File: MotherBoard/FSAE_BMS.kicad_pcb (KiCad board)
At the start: 2 copper layers, 2 parts, among them J1 1376357-3, U1 STM32F205RBTx

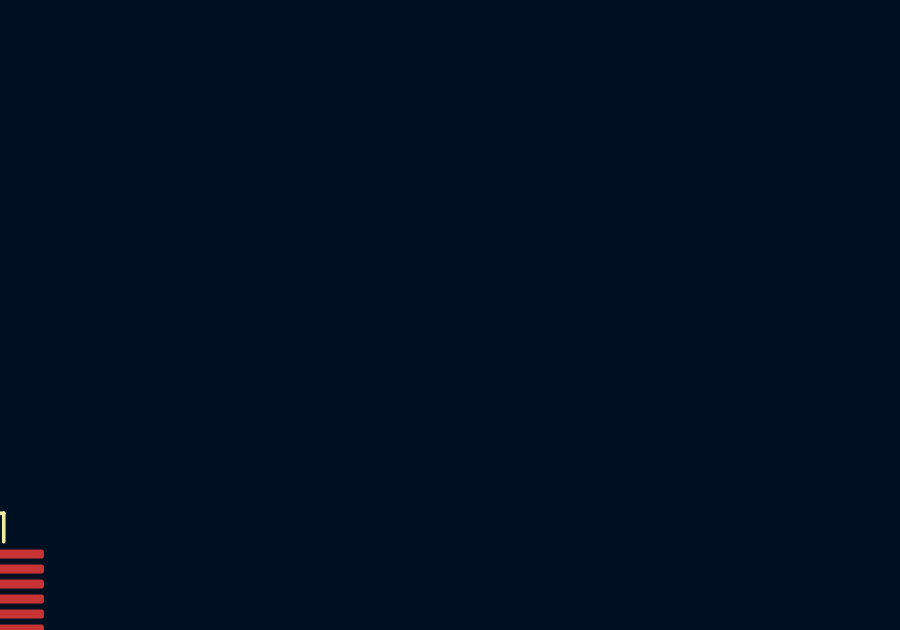
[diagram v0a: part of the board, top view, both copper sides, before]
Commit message: Complete bootstrap schematic for MCU
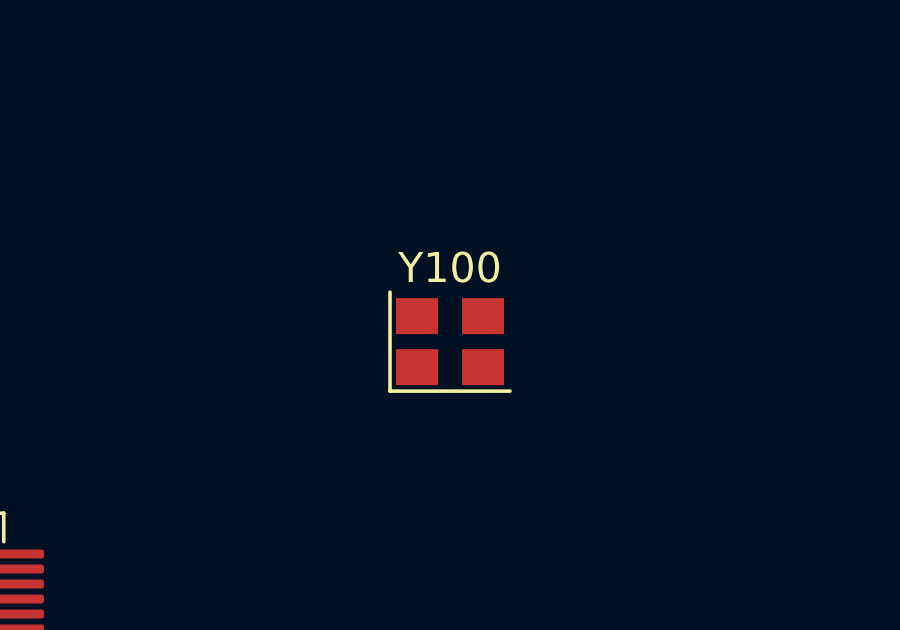
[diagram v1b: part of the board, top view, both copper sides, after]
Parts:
- added Y100: 16 Mhz, Crystal:Crystal_SMD_3225-4Pin_3.2x2.5mm, F.Cu at (136.3, 66.9)
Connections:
- U1 pad 12: unconnected-(U1-VSSA-Pad12) -> GND
- U1 pad 14: unconnected-(U1-PA0-Pad14) -> ADC3_IN0
- U1 pad 15: unconnected-(U1-PA1-Pad15) -> ADC3_IN1
- U1 pad 18: Net-(U1-VSS-Pad18) -> GND
- U1 pad 21: unconnected-(U1-PA5-Pad21) -> SPI1_SCK
- U1 pad 22: unconnected-(U1-PA6-Pad22) -> SPI1_MISO
- U1 pad 23: unconnected-(U1-PA7-Pad23) -> SPI1_MOSI
- U1 pad 24: unconnected-(U1-PC4-Pad24) -> CHARGE_EN_LV
- U1 pad 25: unconnected-(U1-PC5-Pad25) -> DISCHARGE_EN_LV
- U1 pad 26: unconnected-(U1-PB0-Pad26) -> CHARGE_SAFE_LV
- U1 pad 27: unconnected-(U1-PB1-Pad27) -> CHARGE_PWR_CTRL
- U1 pad 28: unconnected-(U1-PB2-Pad28) -> READY_PWR_CTRL
- U1 pad 29: unconnected-(U1-PB10-Pad29) -> FAN_EN
- U1 pad 33: unconnected-(U1-PB12-Pad33) -> CAN2_RX
- U1 pad 34: unconnected-(U1-PB13-Pad34) -> CAN2_TX
- U1 pad 39: unconnected-(U1-PC8-Pad39) -> SDIO_D0
- U1 pad 40: unconnected-(U1-PC9-Pad40) -> SDIO_D1
- U1 pad 41: unconnected-(U1-PA8-Pad41) -> FAN_PWM
- U1 pad 44: unconnected-(U1-PA11-Pad44) -> CAN1_RX
- U1 pad 45: unconnected-(U1-PA12-Pad45) -> CAN1_TX
- U1 pad 46: unconnected-(U1-PA13-Pad46) -> /MCU/SWDIO
- U1 pad 49: unconnected-(U1-PA14-Pad49) -> /MCU/SWCLK
- U1 pad 51: unconnected-(U1-PC10-Pad51) -> SDIO_D2
- U1 pad 52: unconnected-(U1-PC11-Pad52) -> SDIO_D3
- U1 pad 53: unconnected-(U1-PC12-Pad53) -> SDIO_CK
- U1 pad 54: unconnected-(U1-PD2-Pad54) -> SDIO_CMD
- U1 pad 55: unconnected-(U1-PB3-Pad55) -> /MCU/SWO
- U1 pad 63: Net-(U1-VSS-Pad18) -> GND

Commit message: PSU Complete
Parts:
- removed J1: 1376357-3, IO:13763573
- removed U1: STM32F205RBTx, Package_QFP:LQFP-64_10x10mm_P0.5mm
- removed Y100: 16 Mhz, Crystal:Crystal_SMD_3225-4Pin_3.2x2.5mm
- added D201: D_TVS, Diode_SMD:D_SOD-323, F.Cu at (89.1, 47.0)
- added D202: D_TVS, Diode_SMD:D_SOD-323, F.Cu at (89.1, 53.9)
- added D203: D_TVS, Diode_SMD:D_SOD-323, F.Cu at (89.1, 60.7)
- added D204: D_TVS, Diode_SMD:D_SOD-323, F.Cu at (89.1, 67.6)
- added D205: D_TVS, Diode_SMD:D_SOD-323, F.Cu at (89.1, 74.4)
- added D206: D_TVS, Diode_SMD:D_SOD-323, F.Cu at (89.1, 81.3)
- added D207: D_TVS, Diode_SMD:D_SOD-323, F.Cu at (89.1, 88.1)
- added D208: D_TVS, Diode_SMD:D_SOD-323, F.Cu at (89.1, 95.0)
- added D209: D_TVS, Diode_SMD:D_SOD-323, F.Cu at (89.1, 101.8)
- added D210: D_TVS, Diode_SMD:D_SOD-323, F.Cu at (89.1, 108.7)
- added D211: D_TVS, Diode_SMD:D_SOD-323, F.Cu at (89.1, 115.5)
- added D212: D_TVS, Diode_SMD:D_SOD-323, F.Cu at (89.1, 122.4)
- added D213: D_TVS, Diode_SMD:D_SOD-323, F.Cu at (89.1, 129.2)
- added J201: Conn_ARM_SWD_TagConnect_TC2030, Connector:Tag-Connect_TC2030-IDC-FP_2x03_P1.27mm_Vertical, F.Cu at (111.2, 62.8)
- added J301: 1376357-3, IO:13763573, F.Cu at (125.4, 49.8)
- added L402: 22u, SW_Inductor:IND_IHLP-6767DZ_VIS, F.Cu at (176.1, 58.2)
- added L403: 22u, SW_Inductor:IND_IHLP-6767DZ_VIS, F.Cu at (176.1, 77.0)
- added R201: 10k, Resistor_SMD:R_0402_1005Metric, F.Cu at (49.6, 50.1)
- added R202: 0R, Resistor_SMD:R_0402_1005Metric, F.Cu at (49.6, 52.1)
- added R203: 22R, Resistor_SMD:R_0402_1005Metric, F.Cu at (49.6, 54.1)
- added R204: 22R, Resistor_SMD:R_0402_1005Metric, F.Cu at (49.6, 56.1)
- added R205: 22R, Resistor_SMD:R_0402_1005Metric, F.Cu at (49.6, 58.0)
- added R206: 22R, Resistor_SMD:R_0402_1005Metric, F.Cu at (52.5, 50.1)
- added R207: 10k, Resistor_SMD:R_0402_1005Metric, F.Cu at (52.5, 52.1)
- added R208: 10k, Resistor_SMD:R_0402_1005Metric, F.Cu at (52.5, 54.1)
- added R209: 10k, Resistor_SMD:R_0402_1005Metric, F.Cu at (52.5, 56.1)
- added R210: 10k, Resistor_SMD:R_0402_1005Metric, F.Cu at (52.5, 58.0)
- added R211: 10k, Resistor_SMD:R_0402_1005Metric, F.Cu at (55.5, 50.1)
- added R212: 10k, Resistor_SMD:R_0402_1005Metric, F.Cu at (55.5, 52.1)
- added R213: 22R, Resistor_SMD:R_0402_1005Metric, F.Cu at (55.5, 54.1)
- added R214: 1M, Resistor_SMD:R_0402_1005Metric, F.Cu at (55.5, 56.1)
- added R401: 100k, Resistor_SMD:R_0402_1005Metric, F.Cu at (44.7, 50.1)
- added R402: 22.1k, Resistor_SMD:R_0402_1005Metric, F.Cu at (44.7, 52.1)
- added R403: 162k, Resistor_SMD:R_0402_1005Metric, F.Cu at (44.7, 54.1)
- added R404: 22.1k, Resistor_SMD:R_0402_1005Metric, F.Cu at (44.7, 56.1)
- added R405: 1k, Resistor_SMD:R_0402_1005Metric, F.Cu at (44.7, 58.0)
- added R406: 1k, Resistor_SMD:R_0402_1005Metric, F.Cu at (44.7, 60.0)
- added U201: STM32F205RBTx, Package_QFP:LQFP-64_10x10mm_P0.5mm, F.Cu at (113.6, 50.8)
- added U401: LMR51430, Package_TO_SOT_SMD:SOT-23-6, F.Cu at (125.4, 93.6)
- added U402: LMR51430, Package_TO_SOT_SMD:SOT-23-6, F.Cu at (125.4, 98.2)
- added Y201: 16 Mhz, Crystal:Crystal_SMD_3225-4Pin_3.2x2.5mm, F.Cu at (118.1, 60.3)

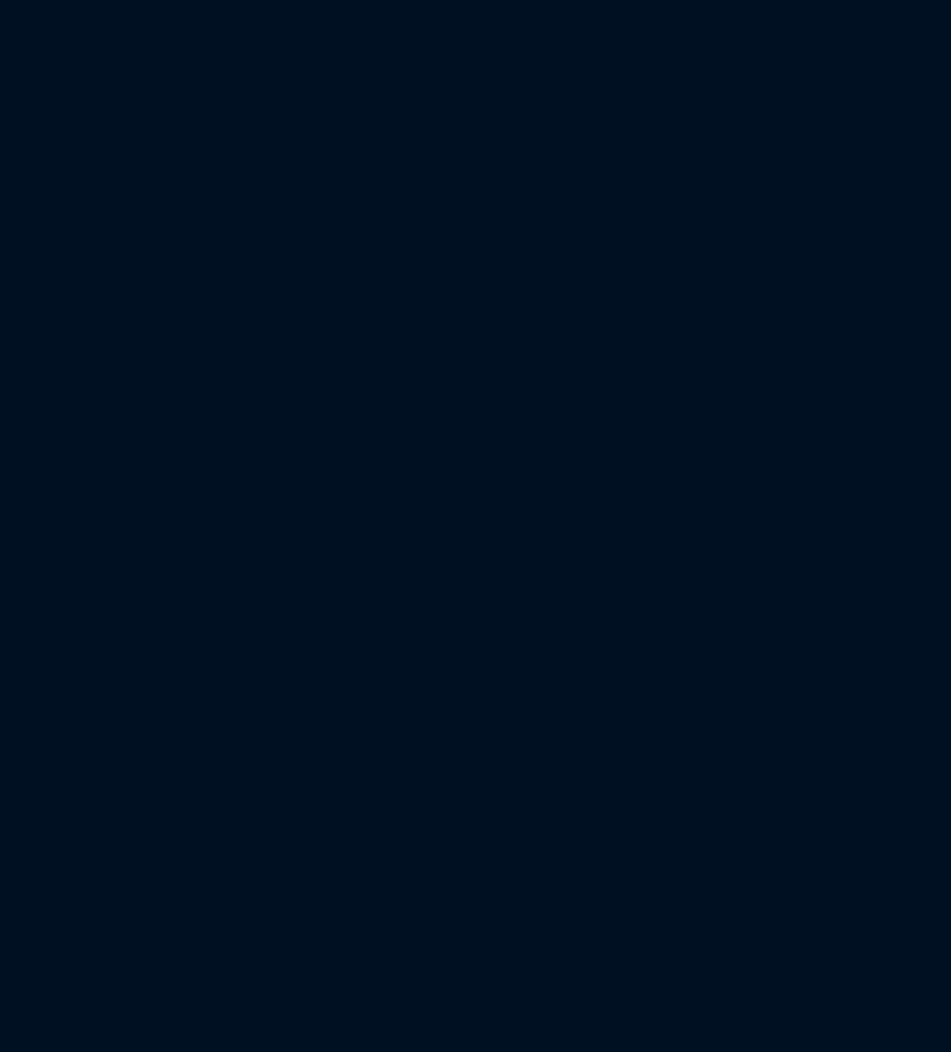
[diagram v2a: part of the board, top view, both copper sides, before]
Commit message: Added BQ7900 rough draft and TCAN
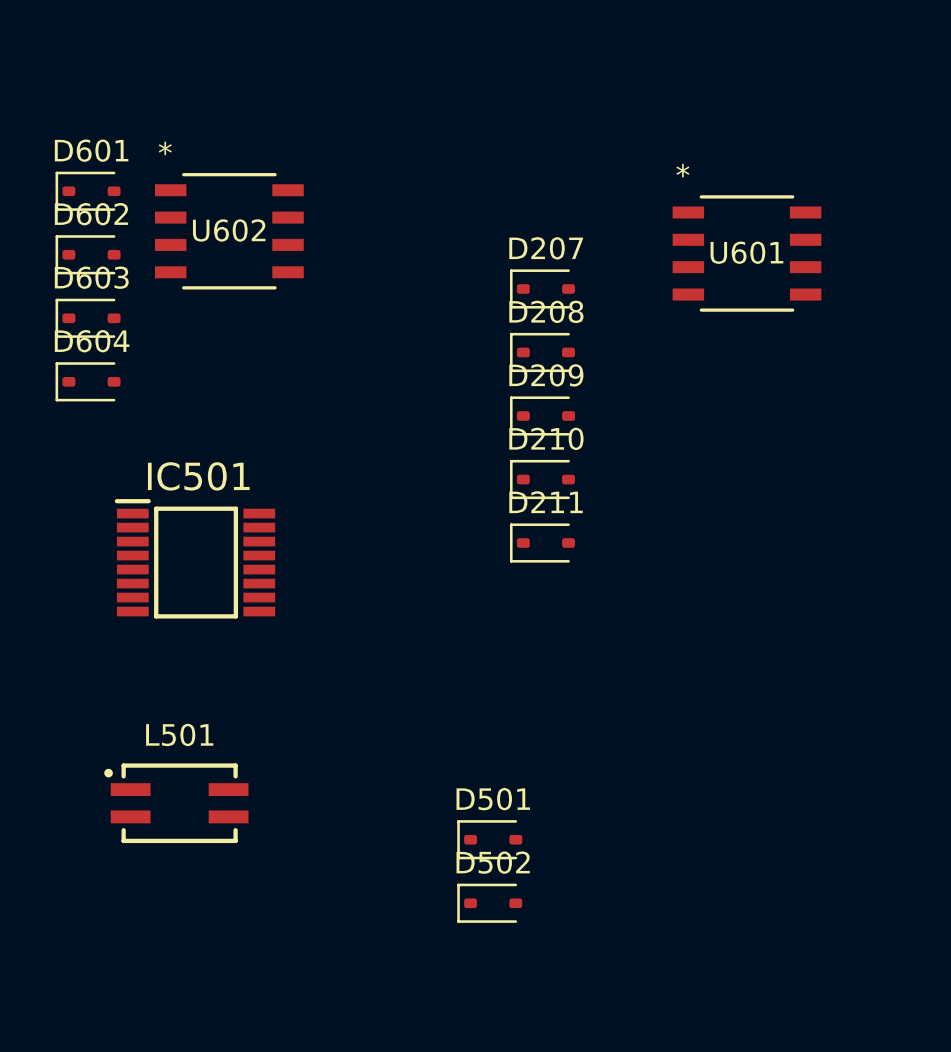
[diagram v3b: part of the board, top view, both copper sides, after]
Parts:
- added D207: D_TVS, Diode_SMD:D_SOD-323, F.Cu at (61.6, 76.1)
- added D208: D_TVS, Diode_SMD:D_SOD-323, F.Cu at (61.6, 79.1)
- added D209: D_TVS, Diode_SMD:D_SOD-323, F.Cu at (61.6, 82.0)
- added D210: D_TVS, Diode_SMD:D_SOD-323, F.Cu at (61.6, 85.0)
- added D211: D_TVS, Diode_SMD:D_SOD-323, F.Cu at (61.6, 87.9)
- added D501: D_TVS, Diode_SMD:D_SOD-323, F.Cu at (59.2, 101.7)
- added D502: D_TVS, Diode_SMD:D_SOD-323, F.Cu at (59.2, 104.7)
- added D601: D_TVS, Diode_SMD:D_SOD-323, F.Cu at (40.5, 71.6)
- added D602: D_TVS, Diode_SMD:D_SOD-323, F.Cu at (40.5, 74.5)
- added D603: D_TVS, Diode_SMD:D_SOD-323, F.Cu at (40.5, 77.5)
- added D604: D_TVS, Diode_SMD:D_SOD-323, F.Cu at (40.5, 80.4)
- added IC501: BQ79600PWRQ1, BQ79600:BQ79600, F.Cu at (45.4, 88.8)
- added L501: WE-SLM, Transformer_WURTH:Isolation_Transformer, F.Cu at (44.6, 100.0)
- added U601: PTCAN1462DRQ1, TCAN:TCAN, F.Cu at (71.0, 74.5)
- added U602: PTCAN1462DRQ1, TCAN:TCAN, F.Cu at (46.9, 73.4)
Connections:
- net SPI_NSS renamed SPI1_NSS
- J301 pad 10: unconnected-(J301-Pad10) -> FAN_EN_CONN
- J301 pad 12: unconnected-(J301-Pad12) -> GND
- J301 pad 18: unconnected-(J301-Pad18) -> CAN1_CONN+
- J301 pad 19: unconnected-(J301-Pad19) -> CAN1_CONN-
- J301 pad 2: unconnected-(J301-Pad2) -> READY_PWR_CONN
- J301 pad 20: unconnected-(J301-Pad20) -> CAN2_CONN-
- J301 pad 21: unconnected-(J301-Pad21) -> CAN2_CONN+
- J301 pad 24: unconnected-(J301-Pad24) -> FAN_PWM_CONN
- J301 pad 3: unconnected-(J301-Pad3) -> CHARGE_PWR_CONN
- J301 pad 6: unconnected-(J301-Pad6) -> CHARGE_SAFE_CONN
- J301 pad 7: unconnected-(J301-Pad7) -> DISCHARGE_EN_CONN
- J301 pad 8: unconnected-(J301-Pad8) -> CHARGE_EN_CONN
- U201 pad 21: SPI1_SCK -> SPI_SCK
- U201 pad 22: SPI1_MISO -> SPI_MISO
- U201 pad 23: SPI1_MOSI -> SPI_MOSI

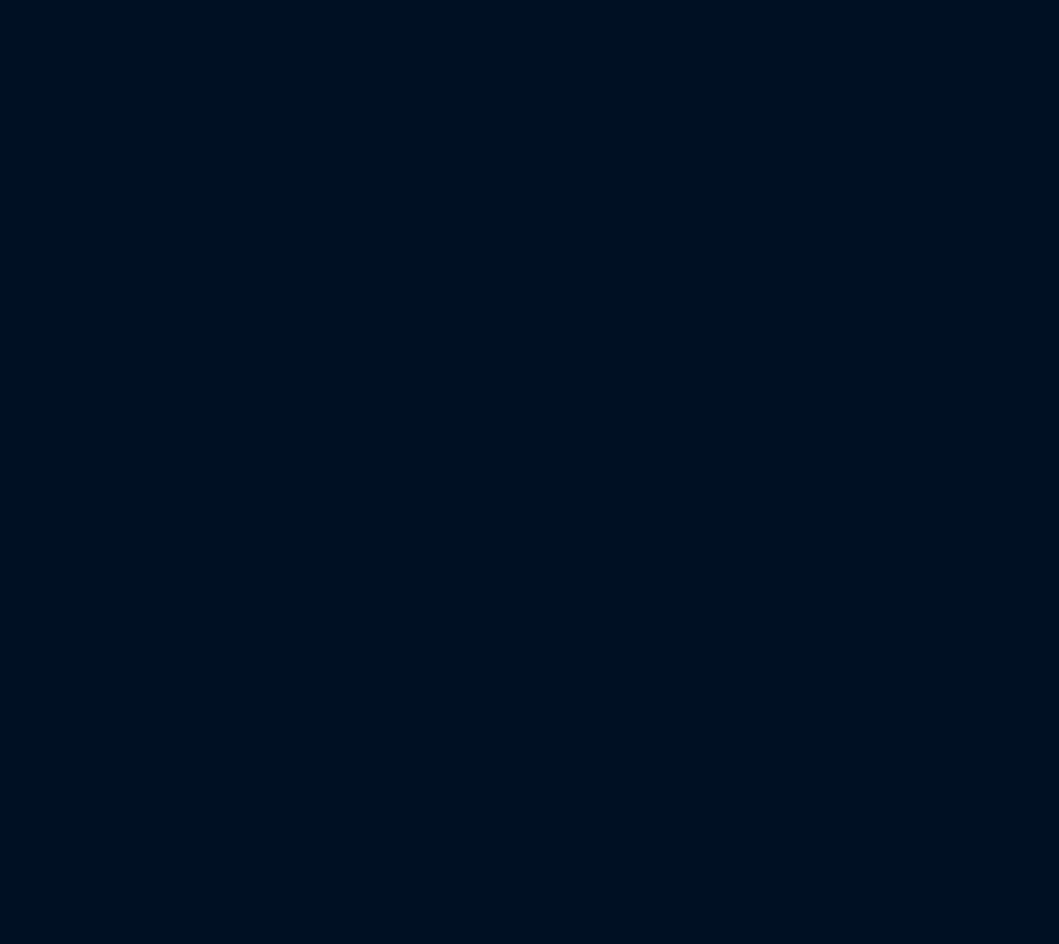
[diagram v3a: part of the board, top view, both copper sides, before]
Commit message: Fixed BQ79600 + minor changes
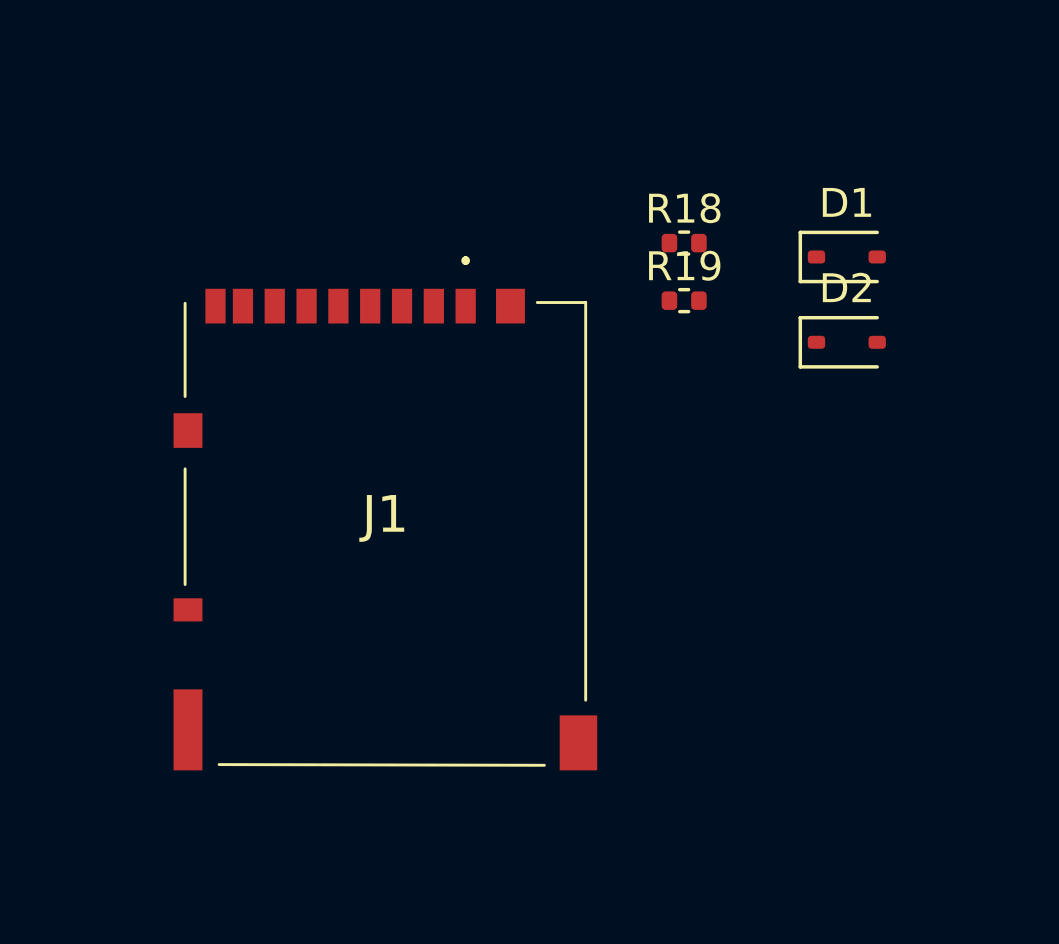
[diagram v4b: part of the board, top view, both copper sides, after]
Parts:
- added D1: D_TVS, Diode_SMD:D_SOD-323, F.Cu at (167.3, 107.7)
- added D2: D_TVS, Diode_SMD:D_SOD-323, F.Cu at (167.3, 110.7)
- added J1: DM3AT-SF-PEJM5_40_, SDIO:SD_CARD, F.Cu at (154.1, 110.0)
- added R18: 0R, Resistor_SMD:R_0402_1005Metric, F.Cu at (161.7, 107.2)
- added R19: 10k, Resistor_SMD:R_0402_1005Metric, F.Cu at (161.7, 109.2)
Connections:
- net Net-(IC501-COMHN) renamed /BQ79600/COMHN
- net Net-(IC501-COMHP) renamed /BQ79600/COMHP
- IC501 pad 1: GND -> Net-(IC501-DVDD)
- IC501 pad 2: unconnected-(IC501-NFAULT-Pad2) -> BQ_NFAULT
- IC501 pad 8: unconnected-(IC501-NUART/SPI_(SPI_RDY)-Pad8) -> BQ_SPI_RDY
- U201 pad 30: unconnected-(U201-PB11-Pad30) -> BQ_NFAULT
- U201 pad 35: unconnected-(U201-PB14-Pad35) -> BQ_SPI_RDY
- U201 pad 41: FAN_PWM -> unconnected-(U201-PA8-Pad41)
- U201 pad 50: unconnected-(U201-PA15-Pad50) -> /MCU/SDIO_DET
